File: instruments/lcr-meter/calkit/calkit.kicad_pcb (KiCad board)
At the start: 2 copper layers, 38 x 193 mm, 45 parts

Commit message: calkit r2: 1 MOhm standard R11 for the 100 kOhm range above 100 kOhm; standards-file docs
R11 RESI PTFR0805B1M00N9 (C5382604, +-0.1 % +-10 ppm/C, 12,184 in stock) on a new row after R9,
hand-specified tracks like every row. Card 38 x 205 mm; DRC 0 violations / 0 unconnected, Kelvin
audit 15/15, position parity PASS. Five cards $117.70 (+$4.06). order_estimate.py now reads the
outline and flags that the fabrication quote is still for 38 x 193 mm.

CHARACTERIZE.md section 1 documents the standards file, which rows calibrate which range, and the
DMM step for R11; section 5 adds R11's phase. Decision recorded in docs/rev-e-plan.md.

Co-Authored-By: Claude Opus 5.5 <noreply@anthropic.com>
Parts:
- removed the R9 at (119.0, 238.0)
- removed the TAB10 at (132.8, 166.0)
- removed the TAB18 at (132.8, 214.0)
- removed the TAB21 at (105.2, 238.0)
- removed the TAB24 at (132.8, 250.0)
- removed the TAB25 at (105.2, 262.0)
- removed the TAB27 at (105.2, 280.0)
- removed the TAB4 at (132.8, 130.0)
- removed the TAB8 at (132.8, 154.0)
- added C1: 100 nF, CalKit:C_1206_3216Metric, F.Cu at (119.0, 262.0)
- added C2: 100 nF, CalKit:C_1206_3216Metric, F.Cu at (113.8, 274.0)
- added C4: 100 nF, CalKit:C_1206_3216Metric, F.Cu at (119.0, 274.0)
- added C5: 100 nF, CalKit:C_1206_3216Metric, F.Cu at (121.6, 274.0)
- added C6: 100 nF, CalKit:C_1206_3216Metric, F.Cu at (124.2, 274.0)
- added R11: 1 MΩ, CalKit:R_0805_2012Metric, F.Cu at (119.0, 250.0)
- added R5: 2 kΩ, CalKit:R_0805_2012Metric, F.Cu at (119.0, 190.0)
- added R6: 4.99 kΩ, CalKit:R_0805_2012Metric, F.Cu at (119.0, 202.0)
- added TAB20: Kelvin tab, CalKit:KelvinTab_9.5x8, F.Cu at (132.8, 226.0)
- added TAB26: Kelvin tab, CalKit:KelvinTab_9.5x8, F.Cu at (132.8, 262.0)
- added TAB28: Kelvin tab, CalKit:KelvinTab_9.5x8, F.Cu at (132.8, 274.0)
- added TAB30: Kelvin tab, CalKit:KelvinTab_9.5x8, F.Cu at (132.8, 292.0)
- R1: renamed from R6; value 4.99 kΩ -> 20 Ω
- R7: renamed from C6; value 100 nF -> 20 kΩ; footprint CalKit:C_1206_3216Metric -> CalKit:R_0805_2012Metric
- R9: renamed from TAB26; value Kelvin tab -> 100 kΩ; footprint CalKit:KelvinTab_9.5x8 -> CalKit:R_0805_2012Metric
- TAB11: renamed from C1; value 100 nF -> Kelvin tab; footprint CalKit:C_1206_3216Metric -> CalKit:KelvinTab_9.5x8
- TAB18: renamed from C3; value 100 nF -> Kelvin tab; footprint CalKit:C_1206_3216Metric -> CalKit:KelvinTab_9.5x8
- TAB23: renamed from R7; value 20 kΩ -> Kelvin tab; footprint CalKit:R_0805_2012Metric -> CalKit:KelvinTab_9.5x8
- TAB27: renamed from R5; value 2 kΩ -> Kelvin tab; footprint CalKit:R_0805_2012Metric -> CalKit:KelvinTab_9.5x8
- TAB29: renamed from C4; value 100 nF -> Kelvin tab; footprint CalKit:C_1206_3216Metric -> CalKit:KelvinTab_9.5x8
- TAB4: renamed from R1; value 20 Ω -> Kelvin tab; footprint CalKit:R_0805_2012Metric -> CalKit:KelvinTab_9.5x8
- TAB9: renamed from C2; value 100 nF -> Kelvin tab; footprint CalKit:C_1206_3216Metric -> CalKit:KelvinTab_9.5x8
- moved TAB9 96.4 mm to (105.2, 166.0), turned to 0 degrees
- moved TAB5 88.4 mm to (105.2, 142.0)
- moved TAB27 85.1 mm to (105.2, 274.0)
- moved TAB11 73.3 mm to (105.2, 178.0)
- moved TAB24 66.0 mm to (132.8, 250.0)
- moved R1 60.0 mm to (119.0, 142.0)
- moved TAB7 60.0 mm to (105.2, 154.0)
- moved TAB18 50.7 mm to (132.8, 214.0), turned to 0 degrees
- moved TAB21 50.2 mm to (105.2, 238.0)
- moved R7 48.3 mm to (119.0, 214.0), turned to 0 degrees
- moved TAB19 48.0 mm to (105.2, 226.0)
- moved TAB12 45.3 mm to (132.8, 178.0)
- moved TAB23 38.5 mm to (105.2, 250.0)
- moved TAB25 36.5 mm to (105.2, 262.0)
- moved TAB13 36.0 mm to (105.2, 190.0)
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- renumbered C5 to C3, TAB14 to TAB10, TAB5 to TAB12, TAB7 to TAB13, TAB12 to TAB14, TAB19 to TAB17, TAB11 to TAB19, TAB28 to TAB21, TAB23 to TAB22, TAB13 to TAB24, TAB22 to TAB25, TAB20 to TAB5, TAB17 to TAB7, TAB9 to TAB8
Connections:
- R1 pad 1: R6_H -> R1_H
- R1 pad 2: R6_L -> R1_L
- R7 pad 1: C2_6_L -> R7_H
- R7 pad 2: C2_6_H -> R7_L
- R9 pad 1: C2_6_L -> R9_H
- R9 pad 2: C2_6_L -> R9_L
- TAB10 pad 1: R5_L -> R3_L
- TAB10 pad 2: R5_L -> R3_L
- TAB11 pad 1: C1_H -> R4_H
- TAB11 pad 2: C1_L -> R4_H
- TAB12 pad 1: R1_H -> R4_L
- TAB12 pad 2: R1_H -> R4_L
- TAB13 pad 1: R2_H -> R5_H
- TAB13 pad 2: R2_H -> R5_H
- TAB14 pad 1: R4_L -> R5_L
- TAB14 pad 2: R4_L -> R5_L
- TAB17 pad 1: R8_H -> R7_H
- TAB17 pad 2: R8_H -> R7_H
- TAB18 pad 1: C2_6_L -> R7_L
- TAB18 pad 2: C2_6_H -> R7_L
- TAB19 pad 1: R4_H -> R8_H
- TAB19 pad 2: R4_H -> R8_H
- TAB21 pad 1: L1_L -> R9_H
- TAB21 pad 2: L1_L -> R9_H
- TAB22 pad 1: C1_H -> R9_L
- TAB22 pad 2: C1_H -> R9_L
- TAB23 pad 1: R7_H -> R11_H
- TAB23 pad 2: R7_L -> R11_H
- TAB24 pad 1: R5_H -> R11_L
- TAB24 pad 2: R5_H -> R11_L
- TAB25 pad 1: R9_L -> C1_H
- TAB25 pad 2: R9_L -> C1_H
- TAB27 pad 1: R5_H -> C2_6_H
- TAB27 pad 2: R5_L -> C2_6_H
- TAB29 pad 1: C2_6_L -> L1_H
- TAB29 pad 2: C2_6_H -> L1_H
- TAB4 pad 1: R1_H -> OPEN_L
- TAB4 pad 2: R1_L -> OPEN_L
- TAB5 pad 1: R8_L -> R1_H
- TAB5 pad 2: R8_L -> R1_H
- TAB7 pad 1: R7_H -> R2_H
- TAB7 pad 2: R7_H -> R2_H
- TAB8 pad 1: R3_H -> R2_L
- TAB8 pad 2: R3_H -> R2_L
- TAB9 pad 1: C2_6_L -> R3_H
- TAB9 pad 2: C2_6_H -> R3_H
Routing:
- net R11_L: track 0.00 -> 23.0 mm, vias 0 -> 1
- net R11_H: track 0.00 -> 23.0 mm, vias 0 -> 1
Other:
- board size 38 x 193 mm -> 38 x 205 mm
- board text added: "1MΩ HIGH-Z STD"
- board text added: "R11 100kΩ RANGE"
- board text added: "R11 = __________"
- board text added: "TEMPER LCR CAL KIT r2"
- board text removed: "TEMPER LCR CAL KIT r1"

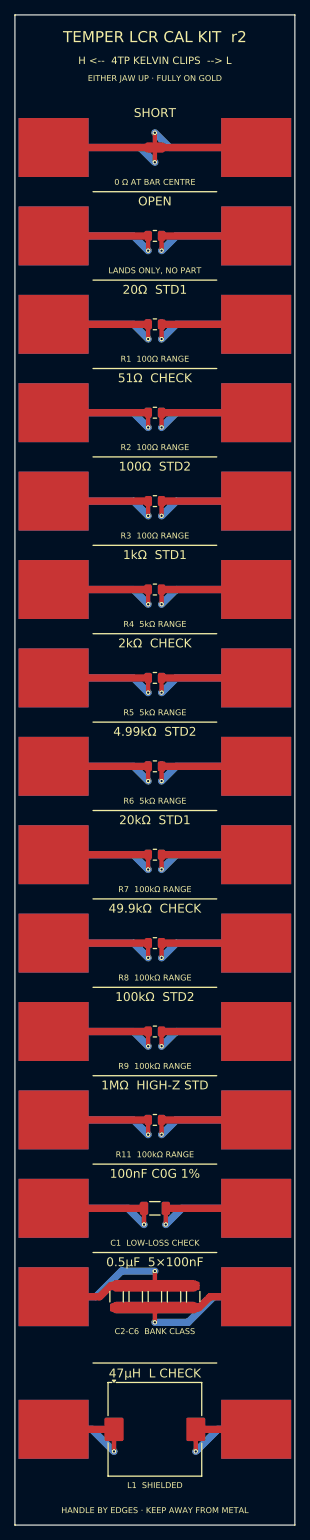
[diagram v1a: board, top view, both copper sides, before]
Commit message: calkit r2: 11 mm row pitch keeps the card at 38 x 191 mm with the 1 MOhm row
The 12 mm pitch (8 mm tab + 4 mm gap) made r2 205 mm long. A 3 mm gap still keeps a centred
jaw up to 14 mm wide off its neighbour, so all 15 rows now fit in 191 mm, 2 mm shorter than r1.
Row labels moved 4.7 -> 4.4 mm from the row centre; R11 label shortened. DRC 0 / 0, Kelvin audit
15/15, position parity PASS. Gold tabs are now 31 % of a face (JLC area-fee threshold 30 %):
re-quote at upload.

Co-Authored-By: Claude Opus 5.5 <noreply@anthropic.com>
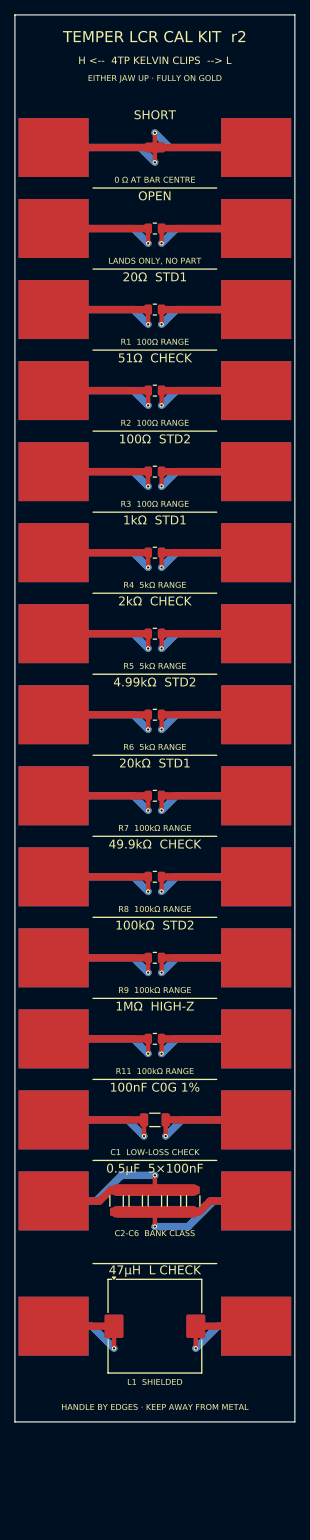
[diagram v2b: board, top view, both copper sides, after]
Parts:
- moved L1 14.0 mm to (119.0, 278.0)
- moved TAB29 14.0 mm to (105.2, 278.0)
- moved TAB30 14.0 mm to (132.8, 278.0)
- moved C2 13.0 mm to (113.8, 261.0)
- moved C3 13.0 mm to (116.4, 261.0)
- moved C4 13.0 mm to (119.0, 261.0)
- moved C5 13.0 mm to (121.6, 261.0)
- moved C6 13.0 mm to (124.2, 261.0)
- moved TAB27 13.0 mm to (105.2, 261.0)
- moved TAB28 13.0 mm to (132.8, 261.0)
- moved C1 12.0 mm to (119.0, 250.0)
- moved TAB25 12.0 mm to (105.2, 250.0)
- moved TAB26 12.0 mm to (132.8, 250.0)
- moved R11 11.0 mm to (119.0, 239.0)
- moved TAB23 11.0 mm to (105.2, 239.0)
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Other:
- board size 38 x 205 mm -> 38 x 191 mm
- board text added: "1MΩ HIGH-Z"
- board text removed: "1MΩ HIGH-Z STD"
